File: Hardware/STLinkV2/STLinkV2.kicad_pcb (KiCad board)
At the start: 2 copper layers, 73.7 x 38.1 mm, 66 parts, among them J1 USB_B_Micro, J2 SWD, J3 RS232, J4 ISP, J5 JTAG, U1 ME6211A33M3, U2 STM32F103CBT6, U3 AD8531ARTZ, U4 TXB0304RUT, U5 TXB0304RUT, Y1 8MHz

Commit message: STLink/V2 (WIP)
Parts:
- moved C11 17.4 mm to (102.6, 80.8), turned to 90 degrees
- moved R1 7.97 mm to (67.2, 75.8), turned to 0 degrees
- moved J1 1.48 mm to (66.2, 69.8)
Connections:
- C30 pad 1: (no net) -> Net-(C29-Pad2)
- C30 pad 2: (no net) -> GND
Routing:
- net /LED: track 0.00 -> 47.9 mm, vias 0 -> 1
- net /STM_NRST: track 27.2 -> 46.8 mm, vias 2 -> 4
- net GND: track 42.3 -> 55.0 mm
- net +3V3: track 48.9 -> 61.7 mm
- net Net-(J1-Pad4): track 0.00 -> 7.88 mm
- net /STM_TDO: track 25.9 -> 32.2 mm
- net /STM_TDI: track 24.7 -> 29.8 mm
- net /STM_TCK: track 27.4 -> 31.2 mm
- net /STM_TMS: track 27.7 -> 26.6 mm
- net Net-(D1-Pad2): track 7.94 -> 8.50 mm

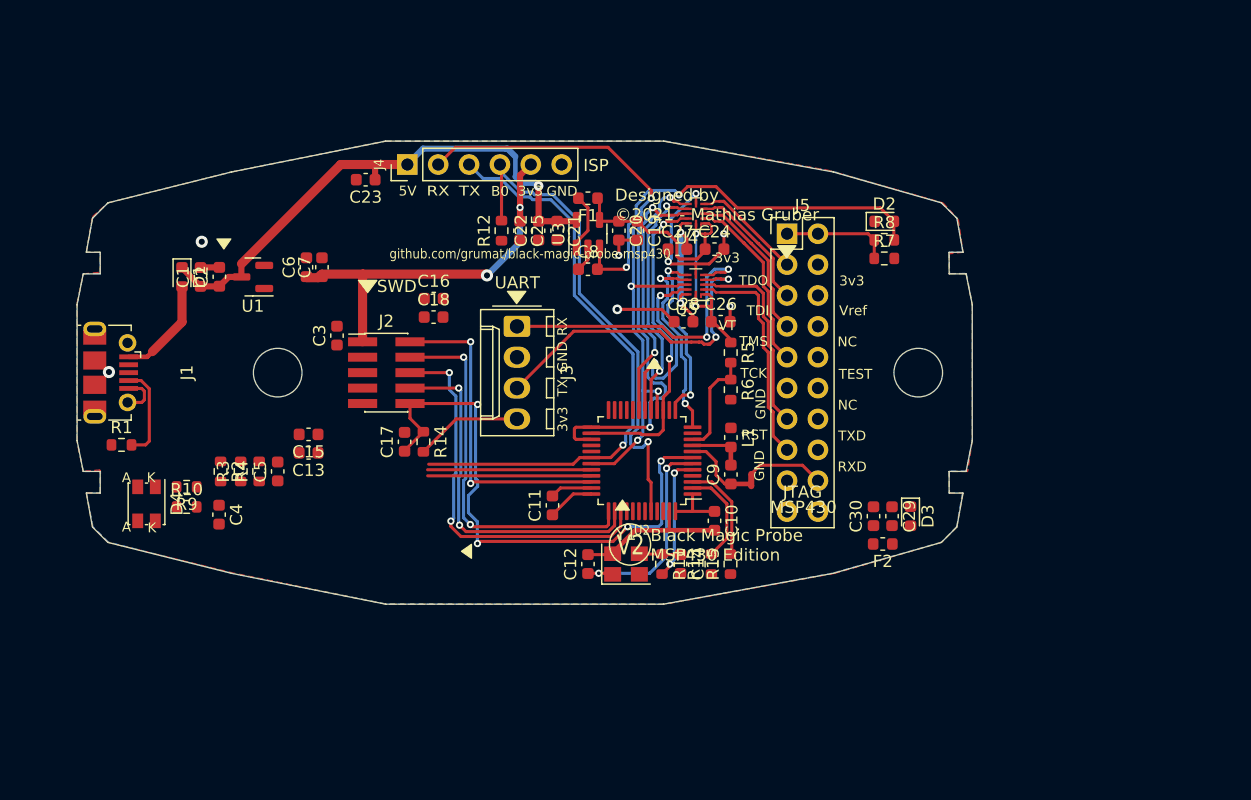
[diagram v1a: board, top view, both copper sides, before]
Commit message: STLink/V2 ready for production
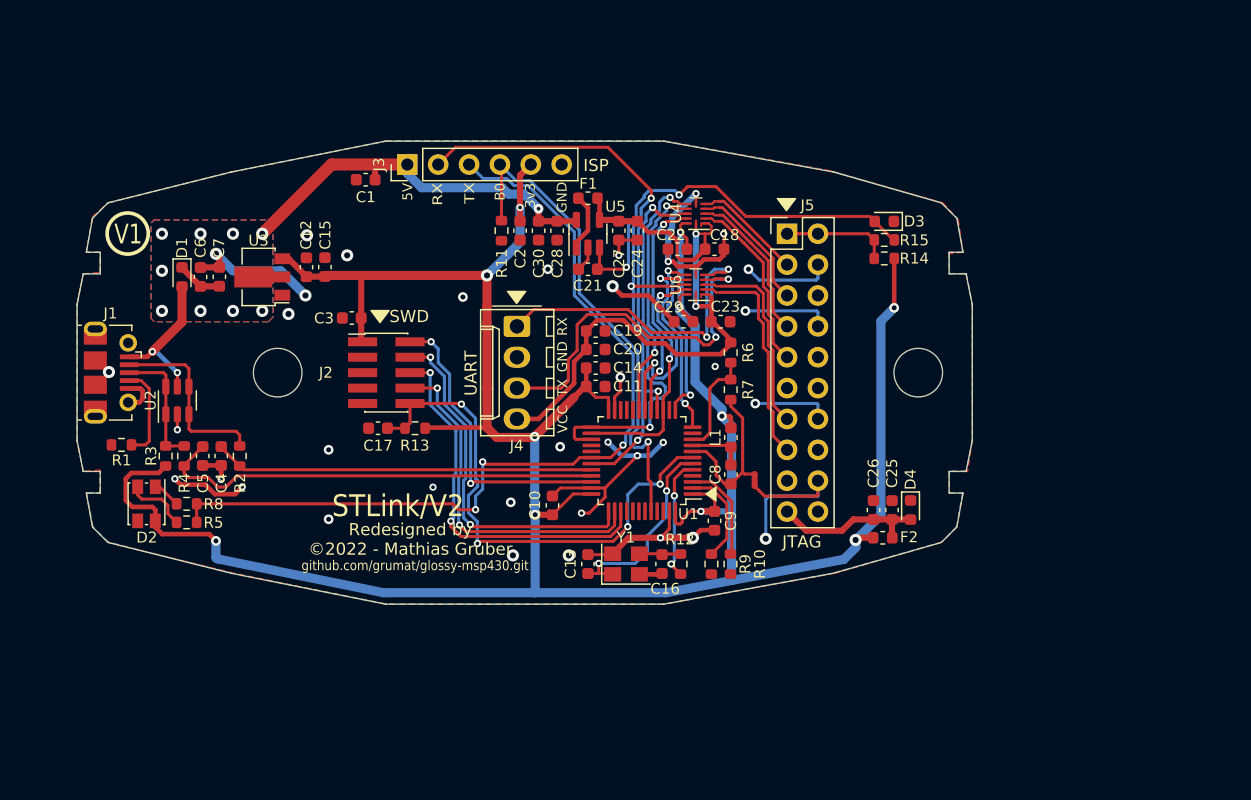
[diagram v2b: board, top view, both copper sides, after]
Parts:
- added U2: SRV05-4, Package_TO_SOT_SMD:SOT-23-6, F.Cu at (71.8, 72.1)
- U3: renamed from U1; value ME6211A33M3 -> HT7833; footprint Package_TO_SOT_SMD:SOT-23 -> Package_TO_SOT_SMD:SOT-89-3
- moved C11 24.2 mm to (106.2, 71.0), turned to 0 degrees
- moved C14 24.2 mm to (106.2, 69.5), turned to 0 degrees
- moved C20 13.6 mm to (106.2, 67.9)
- moved C19 13.6 mm to (106.2, 66.4)
- moved C5 5.01 mm to (73.8, 76.7)
- moved C4 4.82 mm to (75.4, 76.7), turned to -90 degrees
- moved R4 4.82 mm to (72.3, 76.7)
- moved R3 4.70 mm to (70.8, 76.7)
- moved R5 2.92 mm to (72.5, 82.2)
- moved C17 2.45 mm to (88.3, 74.4), turned to 180 degrees
- moved R2 2.04 mm to (76.9, 76.7), turned to -90 degrees
- moved C3 1.89 mm to (86.1, 65.4), turned to 180 degrees
- moved C16 1.52 mm to (111.6, 85.6)
- moved R12 1.52 mm to (113.2, 85.6)
- moved R13 1.31 mm to (91.3, 74.4), turned to 0 degrees
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- renumbered C23 to C1, C11 to C10, C13 to C11, C6 to C12, C12 to C13, C15 to C14, C7 to C15, C14 to C16, C24 to C18, C16 to C19, C25 to C2, C18 to C20, C8 to C21, C27 to C22, C26 to C23, C19 to C24, C29 to C25, C30 to C26, C20 to C27, C21 to C28, C28 to C29, C22 to C30, C5 to C4, C4 to C5, C1 to C6, C2 to C7, C9 to C8, C10 to C9, D4 to D2, D2 to D3, D3 to D4, J4 to J3, J3 to J4, R15 to R10, R12 to R11, R11 to R12, R14 to R13, R7 to R14, R8 to R15, R4 to R2, R2 to R3, R3 to R4, R9 to R5, R5 to R6, R6 to R7, R10 to R8, R13 to R9, U2 to U1, U3 to U5, U5 to U6
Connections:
- net Net-(C29-Pad2) renamed /T3V3
- C18 pad 1: VBUS -> VCC
- C19 pad 1: +3V3 -> VCC
- C20 pad 1: +3V3 -> VCC
- C23 pad 1: VBUS -> VCC
- C24 pad 1: VBUS -> VCC
- C27 pad 1: VBUS -> VCC
- D1 pad 2: Net-(D1-Pad2) -> VBUS
- F1 pad 1: VBUS -> VCC
- J1 pad 1: Net-(D1-Pad2) -> VBUS
- J4 pad 4: +3V3 -> VCC
- R2 pad 1: /USB- -> /E_USB-
- R2 pad 2: /E_USB- -> /USB-
- R6 pad 1: VBUS -> VCC
- R7 pad 2: GND -> GNDA
- U3 pad 2: +3V3 -> +5V
- U3 pad 3: +5V -> +3V3
- U4 pad 1: VBUS -> VCC
- U4 pad 12: VBUS -> VCC
- U5 pad 4: VBUS -> VCC
- U6 pad 1: VBUS -> VCC
- U6 pad 12: VBUS -> VCC
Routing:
- net +3V3: track 61.7 -> 230.8 mm, vias 4 -> 11
- net GND: track 55.0 -> 124.4 mm, vias 8 -> 36
- net VCC: track 0.00 -> 55.7 mm, vias 0 -> 2
- net /LED: track 47.9 -> 72.0 mm, vias 1 -> 3
- net /USB+: track 13.5 -> 37.2 mm
- net VBUS: track 31.1 -> 12.4 mm
- net /USB-: track 13.5 -> 31.3 mm
- net /E_USB-: track 0.00 -> 15.3 mm
- net /T3V3: track 0.00 -> 12.7 mm
- net /E_USB+: track 0.00 -> 10.5 mm
- net Net-(D1-Pad2): track 8.50 -> 0.00 mm
- net GNDA: track 6.66 -> 13.7 mm
- net +5V: track 45.0 -> 39.4 mm, vias 1 -> 10
- net Net-(D2-Pad4): track 0.00 -> 5.20 mm
- net /STM_NRST: track 46.8 -> 43.2 mm
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- added copper zone on B.Cu, net +5V
- added copper zone on F.Cu, net +5V
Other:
- board text added: "Redesigned by ©2022 - Mathias Gruber"
- board text added: "STLink/V2"
- board text added: "V1"
- board text added: "VCC"
- board text added: "github.com/grumat/glossy-msp430.git"
- board text removed: "A"
- board text removed: "Black Magic Probe MSP430 Edition"
- board text removed: "Designed by ©2021 - Mathias Gruber"
- board text removed: "K"
- board text removed: "MSP430"
- board text removed: "NC"
- board text removed: "RST"
- board text removed: "RXD"
- board text removed: "TCK"
- board text removed: "TDI"
- board text removed: "TDO"
- board text removed: "TEST"
- board text removed: "TMS"
- board text removed: "TXD"
- board text removed: "V2"
- board text removed: "VT"
- board text removed: "Vref"
- board text removed: "github.com/grumat/black-magic-probe-msp430"

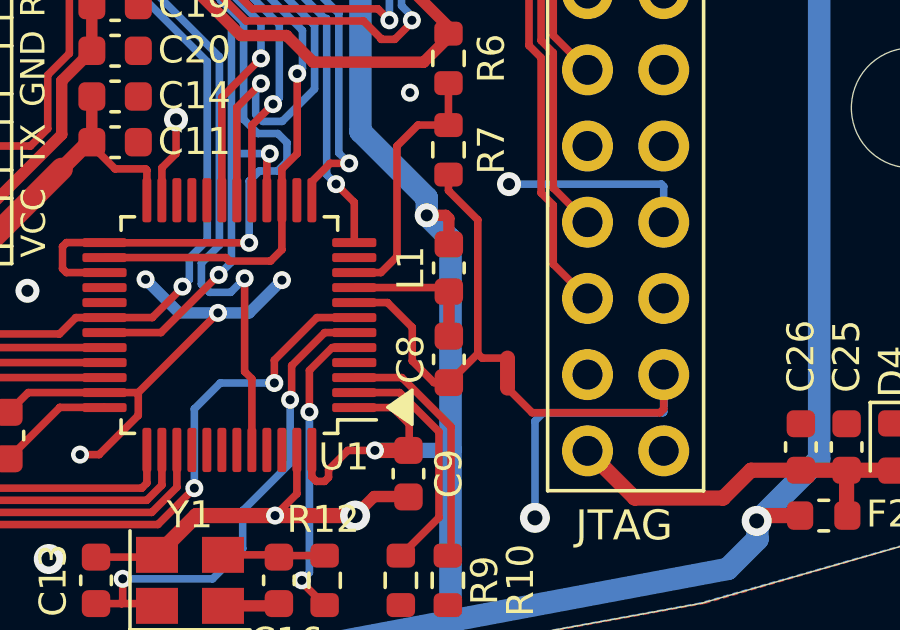
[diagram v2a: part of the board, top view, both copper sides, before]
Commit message: Fine tune of USB EMI filter
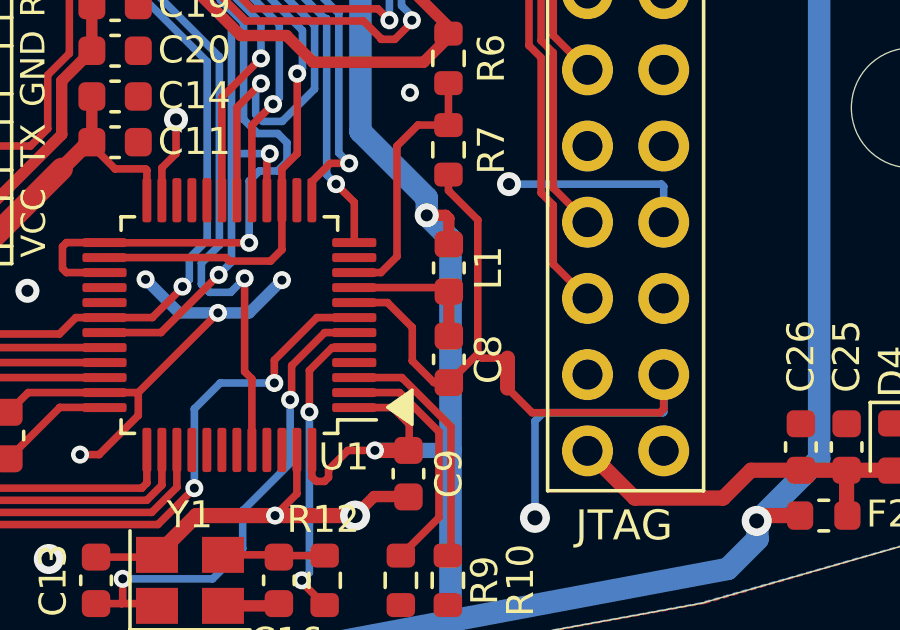
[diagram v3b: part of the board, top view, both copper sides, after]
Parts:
- C4, C5: value 20pF -> 12pF

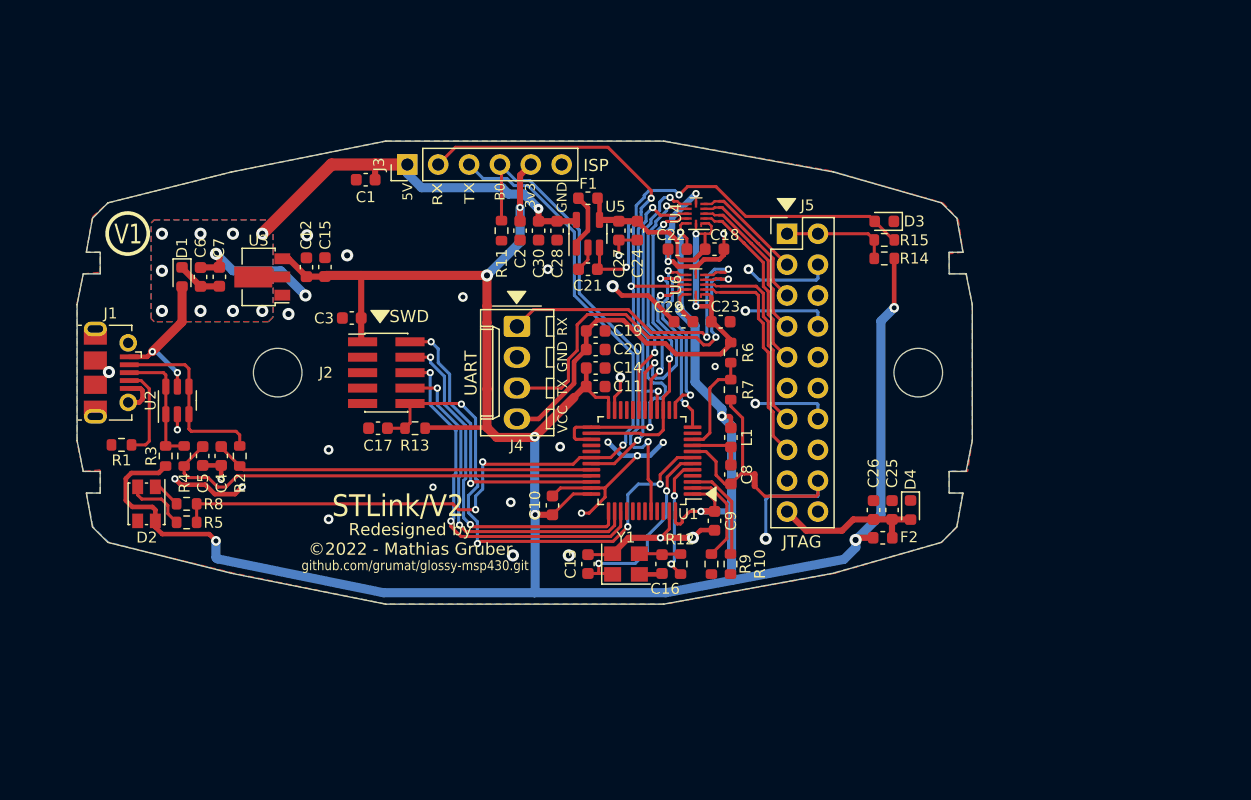
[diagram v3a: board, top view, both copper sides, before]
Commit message: STLink V2 hardware review
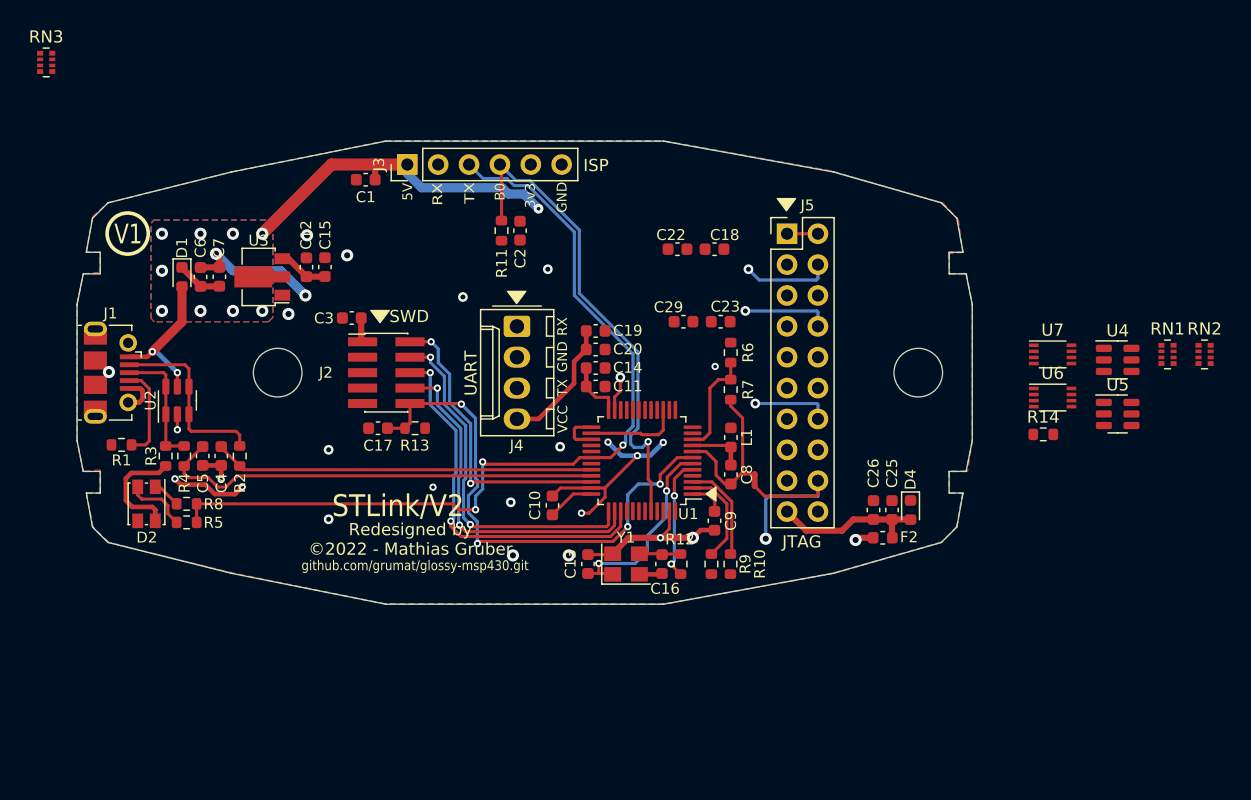
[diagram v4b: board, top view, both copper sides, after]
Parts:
- removed C21, C24, C30: 100nF, Capacitor_SMD:C_0603_1608Metric
- removed C27, C28: 10uF, Capacitor_SMD:C_0603_1608Metric
- removed D3: 82356050050, Diode_SMD:D_0603_1608Metric
- removed F1: Polyfuse, Fuse:Fuse_0603_1608Metric
- removed R15: 100, Resistor_SMD:R_0603_1608Metric
- added RN1: 22, Resistor_SMD:R_Array_Convex_4x0402, F.Cu at (153.2, 68.3)
- added RN2: 22, Resistor_SMD:R_Array_Convex_4x0402, F.Cu at (156.3, 68.3)
- added RN3: 10k, Resistor_SMD:R_Array_Convex_4x0402, F.Cu at (61.0, 44.3)
- added U7: 74AVCH2T45DC,125, Package_SO:VSSOP-8_2.3x2mm_P0.5mm, F.Cu at (143.8, 68.3)
- R14: value 47K -> 10
- U4: value TXB0304RUT -> SRV05-4; footprint Package_DFN_QFN:Texas_R_PUQFN-N12 -> Package_TO_SOT_SMD:SOT-23-6
- U5: value AD8531ARTZ -> SRV05-4; footprint Package_TO_SOT_SMD:SOT-23-5 -> Package_TO_SOT_SMD:SOT-23-6
- U6: value TXB0304RUT -> 74AVCH2T45DC,125; footprint Package_DFN_QFN:Texas_R_PUQFN-N12 -> Package_SO:VSSOP-8_2.3x2mm_P0.5mm
- moved U5 46.0 mm to (149.1, 73.2), turned to 0 degrees
- moved U4 36.7 mm to (149.1, 68.8), turned to 0 degrees
- moved U6 30.8 mm to (143.8, 71.9), turned to 0 degrees
- moved R14 19.5 mm to (143.0, 74.9)
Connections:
- C18 pad 1: VCC -> +3V3
- C19 pad 1: VCC -> /T_VCC
- C20 pad 1: VCC -> /T_VCC
- C22 pad 2: +3V3 -> VCC
- C23 pad 1: VCC -> +3V3
- C29 pad 2: +3V3 -> VCC
- J3 pad 2: /TDO_SWO -> /SWO
- J4 pad 4: VCC -> /T_VCC
- R14 pad 2: +3V3 -> VCC
- U1 pad 16: /TDO_SWO -> /TDO
- U1 pad 25: /TMS_SWDIO -> /TMS
- U1 pad 31: /TDO_SWO -> /SWO
- U4 pad 1: VCC -> /TMS_SWDIO
- U4 pad 2: /T_TCK_SWCLK -> GND
- U4 pad 3: /T_TMS_SWDIO -> /TCK_SWCLK
- U4 pad 4: /T_TDI -> /TRST
- U4 pad 5: /T_TRST -> VCC
- U4 pad 6: GND -> /TDI
- U5 pad 1: Net-(F1-Pad2) -> /TTXD
- U5 pad 3: Net-(C21-Pad2) -> /RXD
- U5 pad 4: VCC -> /TDO_SWO
- U5 pad 5: +5V -> VCC
- U6 pad 1: VCC -> +3V3
- U6 pad 2: /T_NRST -> /TRXD
- U6 pad 3: /T_TDO_SWO -> /TMS
- U6 pad 4: /T_TXD -> GND
- U6 pad 5: /T_RXD -> GND
- U6 pad 6: GND -> /TMS_SWDIO
- U6 pad 7: /TRXD -> /RXD
- U6 pad 8: /TTXD -> VCC
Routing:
- net +3V3: track 230.8 -> 28.5 mm, vias 11 -> 1
- net VCC: track 55.7 -> 0.00 mm, vias 2 -> 0
- net /TDO_SWO: track 53.6 -> 0.00 mm, vias 4 -> 0
- net Net-(C21-Pad2): track 34.2 -> 0.00 mm, vias 2 -> 0
- net /T_TXD: track 30.8 -> 0.00 mm, vias 2 -> 0
- net /TMS_SWDIO: track 32.5 -> 3.65 mm, vias 2 -> 0
- net GND: track 124.4 -> 97.2 mm, vias 36 -> 31
- net /T_RXD: track 26.4 -> 0.00 mm, vias 2 -> 0
- net /TRST: track 21.3 -> 0.00 mm, vias 2 -> 0
- net /TDI: track 20.1 -> 0.00 mm, vias 2 -> 0
- net /TCK_SWCLK: track 26.5 -> 7.77 mm, vias 2 -> 0
- net /T_NRST: track 18.4 -> 0.00 mm
- net /NRST: track 16.7 -> 0.00 mm, vias 2 -> 0
- net /T_TDO_SWO: track 16.3 -> 0.00 mm
- net /TTXD: track 16.1 -> 0.00 mm, vias 2 -> 0
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
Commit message: STLink V2 hardware review
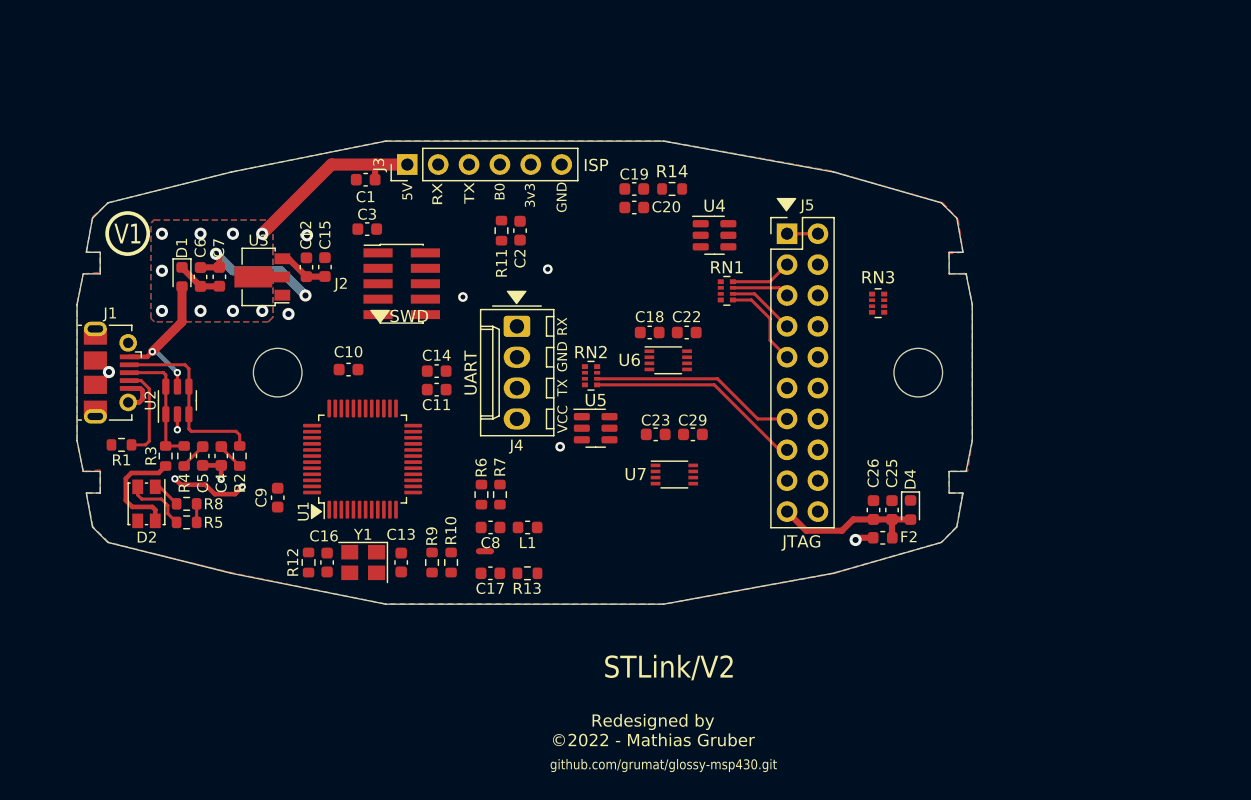
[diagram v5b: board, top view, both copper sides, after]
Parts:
- moved RN3 71.3 mm to (129.4, 64.1)
- moved RN2 50.5 mm to (105.8, 70.1)
- moved U5 43.0 mm to (106.2, 74.4)
- moved RN1 36.6 mm to (117.0, 63.1)
- moved R14 36.6 mm to (112.5, 54.7)
- moved C9 36.0 mm to (80.0, 80.1), turned to 90 degrees
- moved U4 34.7 mm to (116.0, 58.5)
- moved U7 32.7 mm to (112.6, 78.2)
- moved U6 31.8 mm to (112.1, 68.8)
- moved R12 30.6 mm to (82.5, 85.5), turned to 90 degrees
- moved C16 27.6 mm to (84.1, 85.5), turned to 90 degrees
- moved R6 23.6 mm to (96.8, 79.9)
- moved R9 23.0 mm to (92.7, 85.5)
- moved R10 23.0 mm to (94.3, 85.5)
- moved U1 23.0 mm to (87.0, 77.0), turned to 90 degrees
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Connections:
- RN2 pad 1: /TDO_SWO -> /RXD
- RN2 pad 2: /NRST -> /TTXD
- RN2 pad 3: /TTXD -> /TDO_SWO
- RN2 pad 4: /RXD -> /NRST
- RN2 pad 5: /T_RXD -> /T_NRST
- RN2 pad 6: /T_TXD -> /T_TDO_SWO
- RN2 pad 7: /T_NRST -> /T_TXD
- RN2 pad 8: /T_TDO_SWO -> /T_RXD
- U6 pad 2: /TRXD -> /TMS
- U6 pad 3: /TMS -> /TRXD
- U6 pad 6: /TMS_SWDIO -> /RXD
- U6 pad 7: /RXD -> /TMS_SWDIO
- U7 pad 2: /TDO -> /SWO
- U7 pad 3: /SWO -> /TDO
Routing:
- net GND: track 97.2 -> 25.0 mm, vias 31 -> 12
- net /LED: track 72.0 -> 1.52 mm, vias 3 -> 0
- net /STM_NRST: track 43.2 -> 0.00 mm, vias 4 -> 0
- net /BOOT0: track 41.0 -> 0.00 mm, vias 1 -> 0
- net /USB+: track 37.2 -> 2.23 mm
- net /STM_TDO: track 31.3 -> 0.00 mm, vias 2 -> 0
- net /STM_TCK: track 29.6 -> 0.00 mm, vias 2 -> 0
- net /USB-: track 31.3 -> 2.23 mm
- net /STM_TDI: track 28.8 -> 0.00 mm, vias 2 -> 0
- net /STM_TMS: track 24.7 -> 0.00 mm, vias 2 -> 0
- net /T_NRST: track 0.00 -> 17.8 mm
- net /T_TDO_SWO: track 0.00 -> 17.0 mm
- net /OSC_OUT: track 16.6 -> 0.00 mm, vias 2 -> 0
- net GNDA: track 13.7 -> 0.00 mm
- net +3V3: track 28.5 -> 14.8 mm
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
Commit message: ^STLink V2 Hardware review.
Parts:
- removed D4: 82356050050, Diode_SMD:D_0603_1608Metric
- moved R10 14.3 mm to (80.0, 84.7)
- moved R9 14.3 mm to (78.4, 84.7)
- moved C17 4.17 mm to (93.3, 86.4)
- moved R13 4.17 mm to (96.4, 86.4)
- moved R6 1.64 mm to (95.1, 79.9)
- moved R7 1.64 mm to (96.7, 79.9)
- moved C8 1.64 mm to (95.9, 82.6)
- moved L1 1.64 mm to (98.9, 82.6)
- moved NT1 1.64 mm to (95.4, 84.5)
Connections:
- RN2 pad 1: /RXD -> /T_RXD
- RN2 pad 2: /TTXD -> /T_TXD
- RN2 pad 7: /T_TXD -> /TTXD
- RN2 pad 8: /T_RXD -> /RXD
- U5 pad 1: /TTXD -> /NRST
- U5 pad 3: /RXD -> /TDO_SWO
- U5 pad 4: /TDO_SWO -> /TTXD
- U5 pad 5: VCC -> +3V3
- U5 pad 6: /NRST -> /RXD
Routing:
- net /TMS_SWDIO: track 0.00 -> 24.2 mm, vias 0 -> 3
- net +3V3: track 14.8 -> 33.6 mm, vias 1 -> 3
- net GNDA: track 0.00 -> 16.1 mm, vias 0 -> 2
- net /RXD: track 0.00 -> 15.0 mm, vias 0 -> 2
- net +3.3VA: track 0.00 -> 14.4 mm, vias 0 -> 2
- net VCC: track 0.00 -> 12.8 mm, vias 0 -> 2
- net /STM_NRST: track 0.00 -> 11.8 mm
- net /TRST: track 0.00 -> 11.3 mm
- net /VREF2: track 0.00 -> 10.8 mm
- net /TDI: track 0.00 -> 10.7 mm
- net /TCK_SWCLK: track 0.00 -> 10.3 mm
- net /TRXD: track 0.00 -> 10.1 mm, vias 0 -> 1
- net /TMS: track 0.00 -> 9.53 mm, vias 0 -> 1
- net /T_TCK_SWCLK: track 7.45 -> 16.2 mm
- net /TTXD: track 0.00 -> 8.24 mm, vias 0 -> 2
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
